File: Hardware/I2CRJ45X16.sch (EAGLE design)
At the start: 90 parts, among them IC1 MCP23017SO, IC2 MCP23017SO, IC3 MCP23017SO, IC4 MCP23017SO, J1 RJ45-X8, J2 RJ45-X8, J4 I2C-BREAKOUT, J6 I2C-BREAKOUT

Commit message: Replaced project files with major redesign for v3.0 release.
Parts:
- removed C7: 330uF, SuperHouse-DiscreteSemi:CAP_POLG
- removed J6: I2C-BREAKOUT, SuperHouse-Connectors:M02X3-SHROUDED
- added C5: 330uF 50V, SuperHouse-DiscreteSemi:CAP_POLG
- added J3: M01-PLAIN, SuperHouse-Connectors:M01-PLAIN
- added J5: RJ45-X8, SuperHouse-Connectors:RJ45-X8
- FID1, FID2, FID3: device freetronics:FIDUCIAL1X2.5 -> SuperHouse-Symbols:FIDUCIAL1X2.5
- J1, J2: value RJ45-X8 -> I2C-BREAKOUT; device SuperHouse-Connectors:RJ45-X8 -> SuperHouse-Connectors:M02X3-SHROUDED
- J4: value I2C-BREAKOUT -> RJ45-X8; device SuperHouse-Connectors:M02X3-SHROUDED -> SuperHouse-Connectors:RJ45-X8
- LED1: value BLUE -> GREEN
- LED2: value GREEN -> BLUE
- R39, R40: value 4K7 -> 1K
- R65, R66: value 1K -> 4K7
- R67, R68: value 10K -> 4K7
- R69: value 10K -> 22K
- SJ1: value I2C Address -> SDA PU
- SJ3: value SDA PU -> RST-PU; device SuperHouse-Jumpers:SJ-NORMAL -> SuperHouse-Jumpers:SJC-NORMAL
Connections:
- removed net ADDR2: IC1.A2, IC2.A2, IC3.A2, IC4.A2, R67.2, SJ1.1
- new net N$2: R68.2, SJ1.1
- net !INT: now also J3.1
- net !RESET: now also IC1.!RESET, IC2.!RESET, IC3.!RESET, IC4.!RESET, J1.6, J2.6, R69.1; no longer J4.6, J6.6
- net 1A1: now also J4.A1; no longer J1.A1
- net 1A2: now also J4.A2; no longer J1.A2
- net 1A3: now also J4.A3; no longer J1.A3
- net 1A6: now also J4.A6; no longer J1.A6
- net 1B1: now also J4.B1; no longer J1.B1
- net 1B2: now also J4.B2; no longer J1.B2
- net 1B3: now also J4.B3; no longer J1.B3
- net 1B6: now also J4.B6; no longer J1.B6
- net 1C1: now also J4.C1; no longer J1.C1
- net 1C2: now also J4.C2; no longer J1.C2
- net 1C3: now also J4.C3; no longer J1.C3
- net 1C6: now also J4.C6; no longer J1.C6
- net 1D1: now also J4.D1; no longer J1.D1
- net 1D2: now also J4.D2; no longer J1.D2
- net 1D3: now also J4.D3; no longer J1.D3
- net 1D6: now also J4.D6; no longer J1.D6
- net 1E1: now also J4.E1; no longer J1.E1
- net 1E2: now also J4.E2; no longer J1.E2
- net 1E3: now also J4.E3; no longer J1.E3
- net 1E6: now also J4.E6; no longer J1.E6
- net 1F1: now also J4.F1; no longer J1.F1
- net 1F2: now also J4.F2; no longer J1.F2
- net 1F3: now also J4.F3; no longer J1.F3
- net 1F6: now also J4.F6; no longer J1.F6
- net 1G1: now also J4.G1; no longer J1.G1
- net 1G2: now also J4.G2; no longer J1.G2
- net 1G3: now also J4.G3; no longer J1.G3
- net 1G6: now also J4.G6; no longer J1.G6
- net 1H1: now also J4.H1; no longer J1.H1
- net 1H2: now also J4.H2; no longer J1.H2
- net 1H3: now also J4.H3; no longer J1.H3
- net 1H6: now also J4.H6; no longer J1.H6
- net 2A1: now also J5.A1; no longer J2.A1
- net 2A2: now also J5.A2; no longer J2.A2
- net 2A3: now also J5.A3; no longer J2.A3
- net 2A6: now also J5.A6; no longer J2.A6
- net 2B1: now also J5.B1; no longer J2.B1
- net 2B2: now also J5.B2; no longer J2.B2
- net 2B3: now also J5.B3; no longer J2.B3
- net 2B6: now also J5.B6; no longer J2.B6
- net 2C1: now also J5.C1; no longer J2.C1
- net 2C2: now also J5.C2; no longer J2.C2
- net 2C3: now also J5.C3; no longer J2.C3
- net 2C6: now also J5.C6; no longer J2.C6
- net 2D1: now also J5.D1, R40.2; no longer J2.D1, R65.2
- net 2D2: now also J5.D2; no longer J2.D2
- net 2D3: now also J5.D3; no longer J2.D3
- net 2D6: now also J5.D6; no longer J2.D6
- net 2E1: now also J5.E1; no longer J2.E1
- net 2E2: now also J5.E2; no longer J2.E2
- net 2E3: now also J5.E3; no longer J2.E3
- net 2E6: now also J5.E6; no longer J2.E6
- net 2F1: now also J5.F1; no longer J2.F1
- net 2F2: now also J5.F2; no longer J2.F2
- net 2F3: now also J5.F3; no longer J2.F3
- net 2F6: now also J5.F6; no longer J2.F6
- net 2G1: now also J5.G1; no longer J2.G1
- net 2G2: now also J5.G2; no longer J2.G2
- net 2G3: now also J5.G3; no longer J2.G3
- net 2G6: now also J5.G6; no longer J2.G6
- net 2H1: now also J5.H1, R39.2; no longer J2.H1, R66.2
- net 2H2: now also J5.H2; no longer J2.H2
- net 2H3: now also J5.H3; no longer J2.H3
- net 2H6: now also J5.H6; no longer J2.H6
- net GND: now also C5.-, IC1.A2, IC2.A2, IC3.A2, IC4.A2, J1.4, J2.4, J4.A7, J4.A8, J4.B7, J4.B8, J4.C7, J4.C8, J4.D7, J4.D8, J4.E7, J4.E8, J4.F7, J4.F8, J4.G7, J4.G8, J4.GND0, J4.GND1, J4.GND2, J4.GND3, J4.GND4, J4.GND5, J4.H7, J4.H8, J5.A7, J5.A8, J5.B7, J5.B8, J5.C7, J5.C8, J5.D7, J5.D8, J5.E7, J5.E8, J5.F7, J5.F8, J5.G7, J5.G8, J5.GND0, J5.GND1, J5.GND2, J5.GND3, J5.GND4, J5.GND5, J5.H7, J5.H8; no longer C7.-, J1.A7, J1.A8, J1.B7, J1.B8, J1.C7, J1.C8, J1.D7, J1.D8, J1.E7, J1.E8, J1.F7, J1.F8, J1.G7, J1.G8, J1.GND0, J1.GND1, J1.GND2, J1.GND3, J1.GND4, J1.GND5, J1.H7, J1.H8, J2.A7, J2.A8, J2.B7, J2.B8, J2.C7, J2.C8, J2.D7, J2.D8, J2.E7, J2.E8, J2.F7, J2.F8, J2.G7, J2.G8, J2.GND0, J2.GND1, J2.GND2, J2.GND3, J2.GND4, J2.GND5, J2.H7, J2.H8, J4.4, J6.4, R67.1
- net GPB0-4: now also R40.1; no longer R65.1
- net GPB4-4: now also R39.1; no longer R66.1
- net N$1: now also R67.2; no longer R68.2
- net N$7: now also LED2.A, R65.1; no longer LED1.A, R39.1
- net N$8: now also LED1.A, R66.1; no longer LED2.A, R40.1
- net SCL: now also J1.1, J2.1, R67.1; no longer J4.1, J6.1, R68.1
- net SDA: now also J1.2, J2.2, R68.1; no longer J4.2, J6.2, R69.1
- net VCC: now also J1.5, J2.5, R65.2; no longer IC1.!RESET, IC2.!RESET, IC3.!RESET, IC4.!RESET, J4.5, J6.5, R39.2
- net VIN: now also C5.+, J1.3, J2.3, J4.A4, J4.A5, J4.B4, J4.B5, J4.C4, J4.C5, J4.D4, J4.D5, J4.E4, J4.E5, J4.F4, J4.F5, J4.G4, J4.G5, J4.H4, J4.H5, J5.A4, J5.A5, J5.B4, J5.B5, J5.C4, J5.C5, J5.D4, J5.D5, J5.E4, J5.E5, J5.F4, J5.F5, J5.G4, J5.G5, J5.H4, J5.H5, R66.2; no longer C7.+, J1.A4, J1.A5, J1.B4, J1.B5, J1.C4, J1.C5, J1.D4, J1.D5, J1.E4, J1.E5, J1.F4, J1.F5, J1.G4, J1.G5, J1.H4, J1.H5, J2.A4, J2.A5, J2.B4, J2.B5, J2.C4, J2.C5, J2.D4, J2.D5, J2.E4, J2.E5, J2.F4, J2.F5, J2.G4, J2.G5, J2.H4, J2.H5, J4.3, J6.3, R40.2
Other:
- note added: "16-Channel I2C RJ45 Breakout"
- note added: "I2C Addr: 0x20"
- note added: "I2C Addr: 0x21"
- note added: "I2C Addr: 0x22"
- note added: "I2C Addr: 0x23"
- note added: "I2C Addresses: 0x20-0x25"
- note added: "I2C Headers"
- note added: "I2C Pullups"
- note added: "I2C pullups are disabled by default. Solder bridge across SJ2 and SJ3 to enable. Reset pullup is enabled by default. Cut track between pads to disable."
- note added: "MCP23017 Interrupt Output"
- note added: "Power"
- note added: "RJ45 Pinout: 1: Data 1 2: Data 2 3: Data 3 4: VIN 5: VIN 6: Data 4 7: GND 8: GND"
- note added: "Reset Pullup"
- note added: "V3.0 (2021-04-15)"
- note added: "VIN: 12V VCC: 1.8-5.5V"
- note removed: "100: 0x24 101: 0x25 110: 0x26 111: 0x27"
- note removed: "16 Channel I2C RJ45 Breakout"
- note removed: "5: VCC 6: Data 4 7: GND 8: GND"
- note removed: "External Power"
- note removed: "I2C Addr: 0x20/0x24"
- note removed: "I2C Addr: 0x21-0x24 or 0x25-0x27"
- note removed: "I2C Addr: 0x21/0x25"
- note removed: "I2C Addr: 0x22/0x26"
- note removed: "I2C Addr: 0x23/0x27"
- note removed: "I2C Addresses A2 A1 A0 000: 0x20 001: 0x21 010: 0x22 011: 0x23"
- note removed: "I2C Breakouts"
- note removed: "Pullups"
- note removed: "RJ45 Pins 1: Data 1 2: Data 2 3: Data 3 4: VCC"
- note removed: "V1.0 (2019-08-15)"

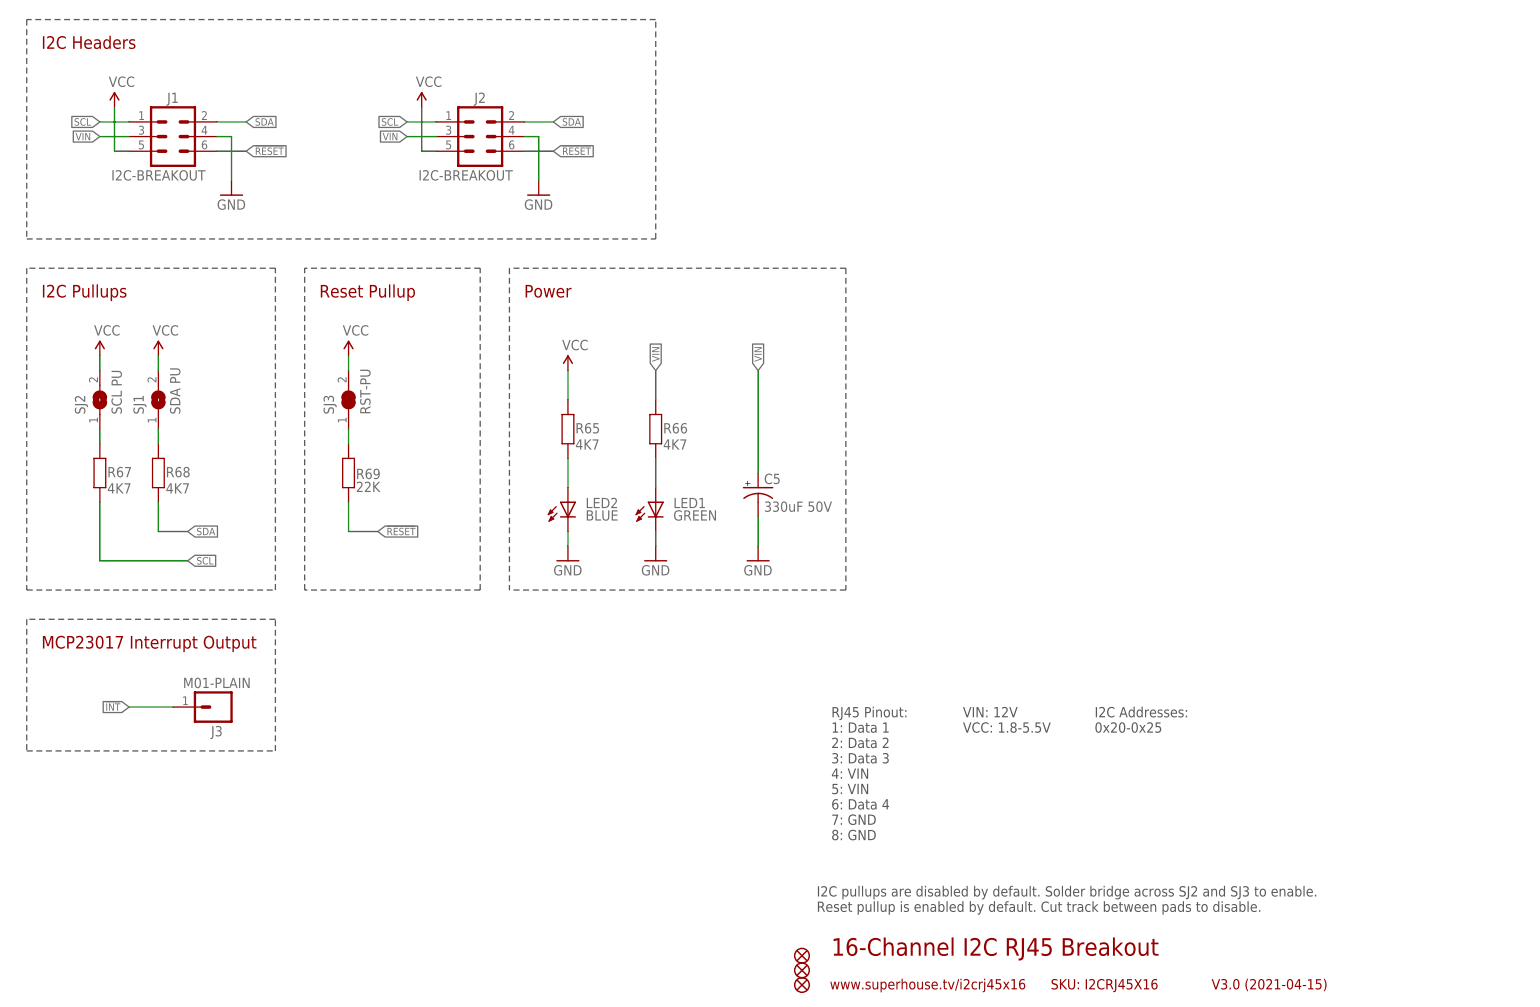
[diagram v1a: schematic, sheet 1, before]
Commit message: Major rework based on 24-port version.
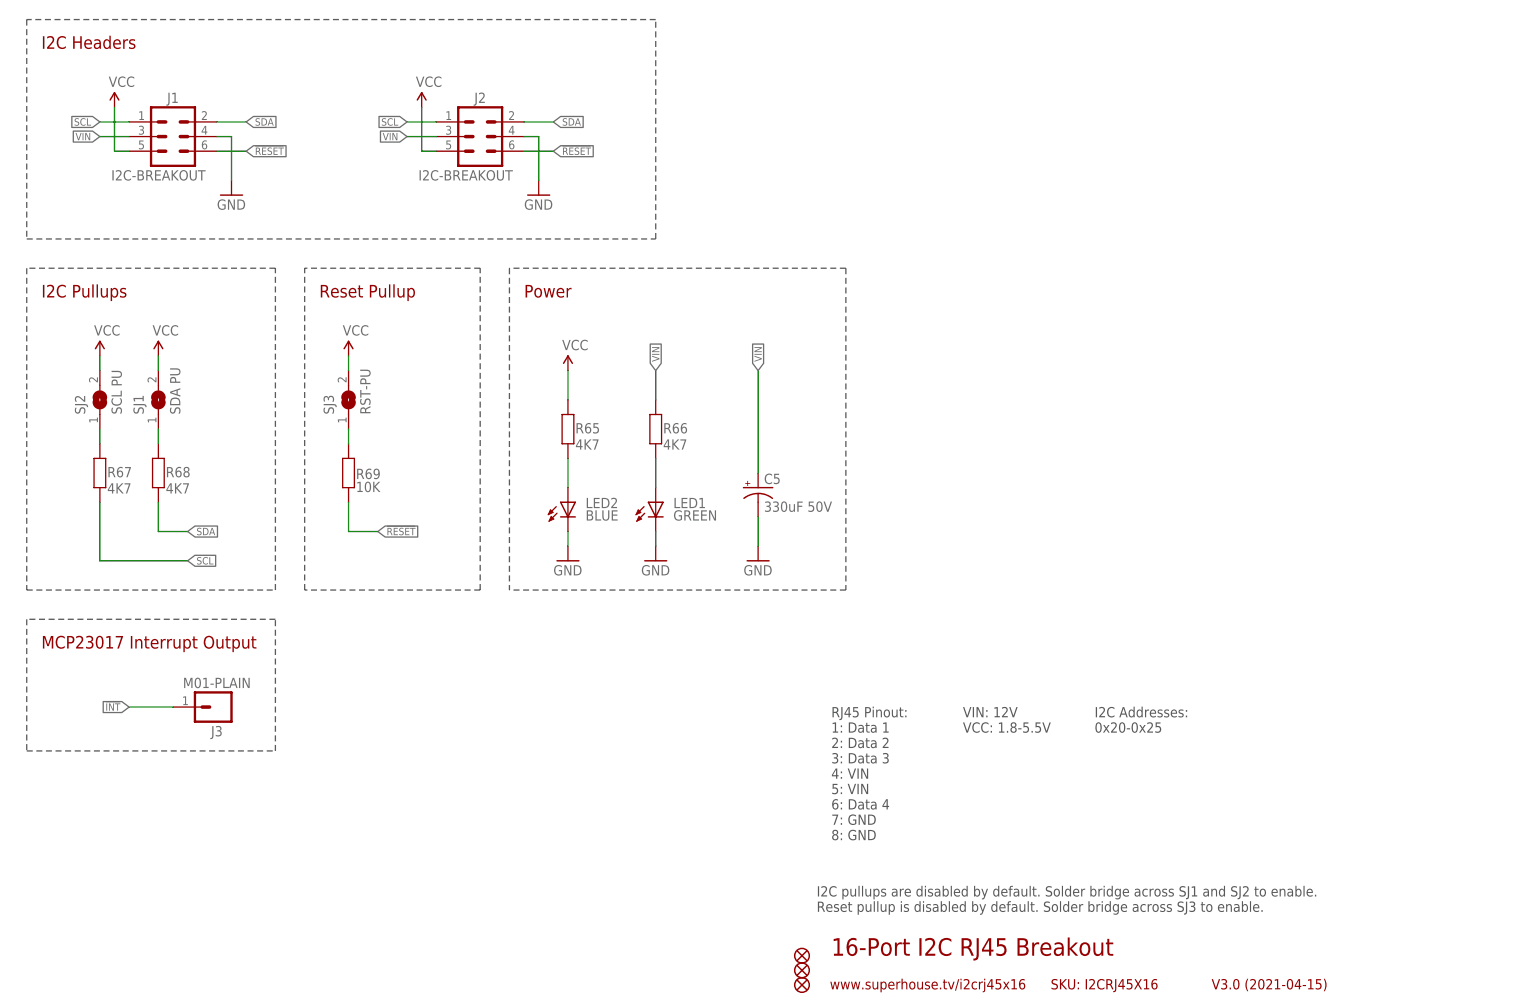
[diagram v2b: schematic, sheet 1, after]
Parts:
- R69: value 22K -> 10K
- SJ3: device SuperHouse-Jumpers:SJC-NORMAL -> SuperHouse-Jumpers:SJ-NORMAL
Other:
- note added: "16-Port I2C RJ45 Breakout"
- note added: "I2C pullups are disabled by default. Solder bridge across SJ1 and SJ2 to enable. Reset pullup is disabled by default. Solder bridge across SJ3 to enable."
- note removed: "16-Channel I2C RJ45 Breakout"
- note removed: "I2C pullups are disabled by default. Solder bridge across SJ2 and SJ3 to enable. Reset pullup is enabled by default. Cut track between pads to disable."
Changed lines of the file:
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@@
 <part name="C3" library="SuperHouse-DiscreteSemi" library_urn="urn:adsk.eagle:library:11768461" deviceset="CAP" device="0805" package3d_urn="urn:adsk.eagle:package:7066318/4" value="10uF"/>
 <part name="C4" library="SuperHouse-DiscreteSemi" library_urn="urn:adsk.eagle:library:11768461" deviceset="CAP" device="0805" package3d_urn="urn:adsk.eagle:package:7066318/4" value="10uF"/>
-<part name="SJ2" library="SuperHouse-Jumpers" library_urn="urn:adsk.eagle:library:12190622" deviceset="SJ" device="-NORMAL" package3d_urn="urn:adsk.eagle:package:7066338/1" value="SCL PU"/>
-<part name="SJ1" library="SuperHouse-Jumpers" library_urn="urn:adsk.eagle:library:12190622" deviceset="SJ" device="-NORMAL" package3d_urn="urn:adsk.eagle:package:7066338/1" value="SDA PU"/>
+<part name="SJ2" library="SuperHouse-Jumpers" library_urn="urn:adsk.eagle:library:12190622" deviceset="SJ" device="-NORMAL" package3d_urn="urn:adsk.eagle:package:7066338/2" value="SCL PU"/>
+<part name="SJ1" library="SuperHouse-Jumpers" library_urn="urn:adsk.eagle:library:12190622" deviceset="SJ" device="-NORMAL" package3d_urn="urn:adsk.eagle:package:7066338/2" value="SDA PU"/>
 <part name="P+8" library="SuperHouse-SupplySymbols" library_urn="urn:adsk.eagle:library:11790503" deviceset="VCC" device=""/>
 <part name="P+9" library="SuperHouse-SupplySymbols" library_urn="urn:adsk.eagle:library:11790503" deviceset="VCC" device=""/>
@@
 <part name="GND10" library="SuperHouse-SupplySymbols" library_urn="urn:adsk.eagle:library:11790503" deviceset="GND" device=""/>
 <part name="GND14" library="SuperHouse-SupplySymbols" library_urn="urn:adsk.eagle:library:11790503" deviceset="GND" device=""/>
-<part name="R69" library="SuperHouse-DiscreteSemi" library_urn="urn:adsk.eagle:library:11768461" deviceset="RESISTOR" device="0603" package3d_urn="urn:adsk.eagle:package:11768543/2" value="22K"/>
+<part name="R69" library="SuperHouse-DiscreteSemi" library_urn="urn:adsk.eagle:library:11768461" deviceset="RESISTOR" device="0603" package3d_urn="urn:adsk.eagle:package:11768543/2" value="10K"/>
 <part name="P+12" library="SuperHouse-SupplySymbols" library_urn="urn:adsk.eagle:library:11790503" deviceset="VCC" device=""/>
-<part name="SJ3" library="SuperHouse-Jumpers" library_urn="urn:adsk.eagle:library:12190622" deviceset="SJC" device="-NORMAL" package3d_urn="urn:adsk.eagle:package:7066342/2" value="RST-PU"/>
+<part name="SJ3" library="SuperHouse-Jumpers" library_urn="urn:adsk.eagle:library:12190622" deviceset="SJ" device="-NORMAL" package3d_urn="urn:adsk.eagle:package:7066338/2" value="RST-PU"/>
 </parts>
 <sheets>
@@
 <plain>
 <frame x1="0" y1="0" x2="248.92" y2="185.42" columns="8" rows="5" layer="94"/>
-<text x="149.86" y="12.7" size="3.048" layer="94">16-Channel I2C RJ45 Breakout</text>
+<text x="149.86" y="12.7" size="3.048" layer="94">16-Port I2C RJ45 Breakout</text>
 <text x="215.9" y="6.858" size="1.778" layer="94">V3.0 (2021-04-15)</text>
 <text x="149.606" y="6.858" size="1.778" layer="94">www.superhouse.tv/i2crj45x16</text>
@@
 <wire x1="119.38" y1="137.16" x2="119.38" y2="175.26" width="0.2032" layer="97" style="longdash"/>
 <wire x1="119.38" y1="175.26" x2="10.16" y2="175.26" width="0.2032" layer="97" style="longdash"/>
-<text x="147.32" y="20.32" size="1.778" layer="97">I2C pullups are disabled by default. Solder bridge across SJ2 and SJ3 to enable.
-Reset pullup is enabled by default. Cut track between pads to disable.</text>
+<text x="147.32" y="20.32" size="1.778" layer="97">I2C pullups are disabled by default. Solder bridge across SJ1 and SJ2 to enable.
+Reset pullup is disabled by default. Solder bridge across SJ3 to enable.</text>
 <wire x1="93.98" y1="132.08" x2="93.98" y2="76.2" width="0.2032" layer="97" style="longdash"/>
 <wire x1="152.4" y1="132.08" x2="93.98" y2="132.08" width="0.2032" layer="97" style="longdash"/>
@@
 <attribute name="VALUE" x="65.024" y="120.396" size="1.778" layer="96"/>
 </instance>
-<instance part="SJ3" gate="G$1" x="66.04" y="109.22" smashed="yes" rot="R90">
+<instance part="SJ3" gate="1" x="66.04" y="109.22" smashed="yes" rot="R90">
 <attribute name="NAME" x="63.5" y="106.68" size="1.778" layer="95" rot="R90"/>
 <attribute name="VALUE" x="69.85" y="106.68" size="1.778" layer="96" rot="R90"/>
@@
 <segment>
 <pinref part="P+12" gate="1" pin="VCC"/>
-<pinref part="SJ3" gate="G$1" pin="2"/>
+<pinref part="SJ3" gate="1" pin="2"/>
 <wire x1="66.04" y1="114.3" x2="66.04" y2="116.84" width="0.1524" layer="91"/>
 </segment>
@@
 <segment>
 <pinref part="R69" gate="G$1" pin="2"/>
-<pinref part="SJ3" gate="G$1" pin="1"/>
+<pinref part="SJ3" gate="1" pin="1"/>
 <wire x1="66.04" y1="101.6" x2="66.04" y2="104.14" width="0.1524" layer="91"/>
 </segment>
